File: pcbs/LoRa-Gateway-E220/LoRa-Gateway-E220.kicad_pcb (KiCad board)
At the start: 2 copper layers, 65.4 x 63 mm, 15 parts, among them J1 Conn_01x02, U1 ESP32_DevKit_V1_DOIT, U2 E-Byte-E220-900T22S, U3 QuinLED-ESP32-ETH-Hat

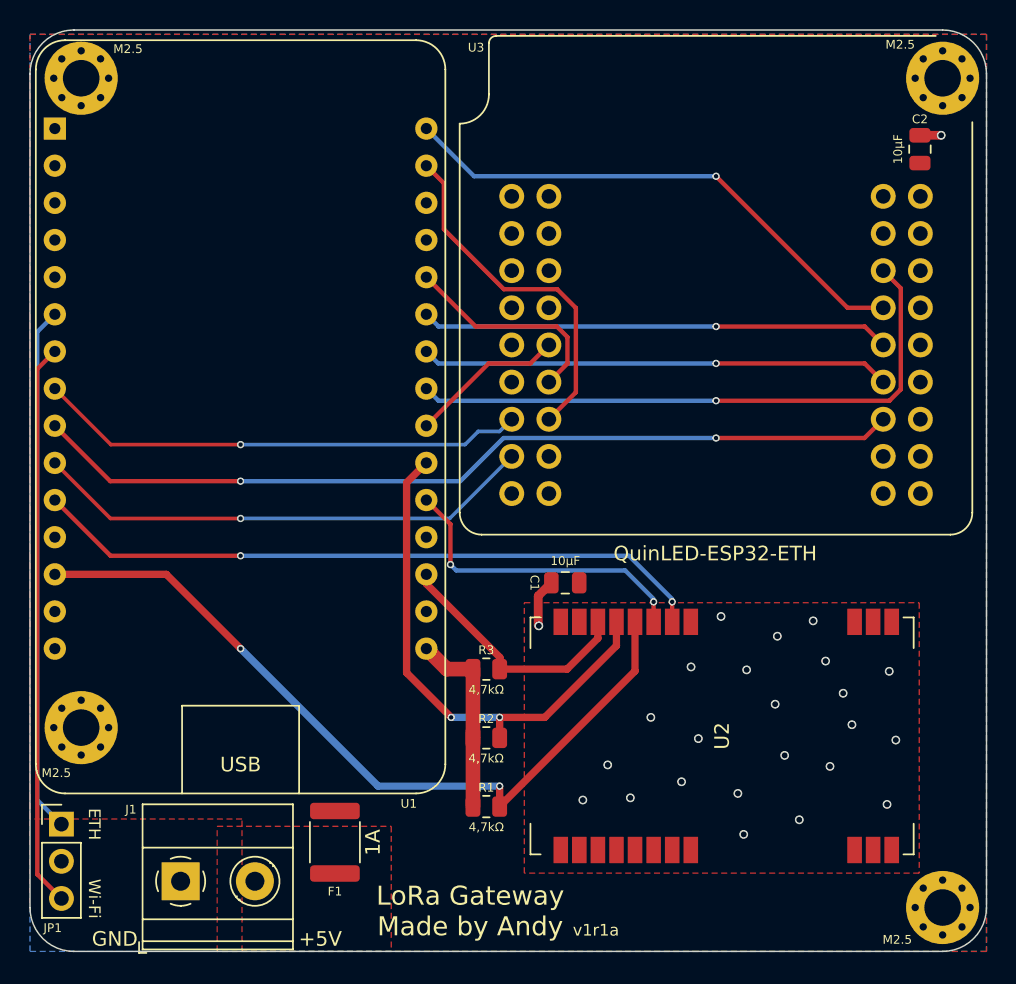
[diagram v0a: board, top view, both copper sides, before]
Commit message: Added iBOM, last small edits on both PCBs
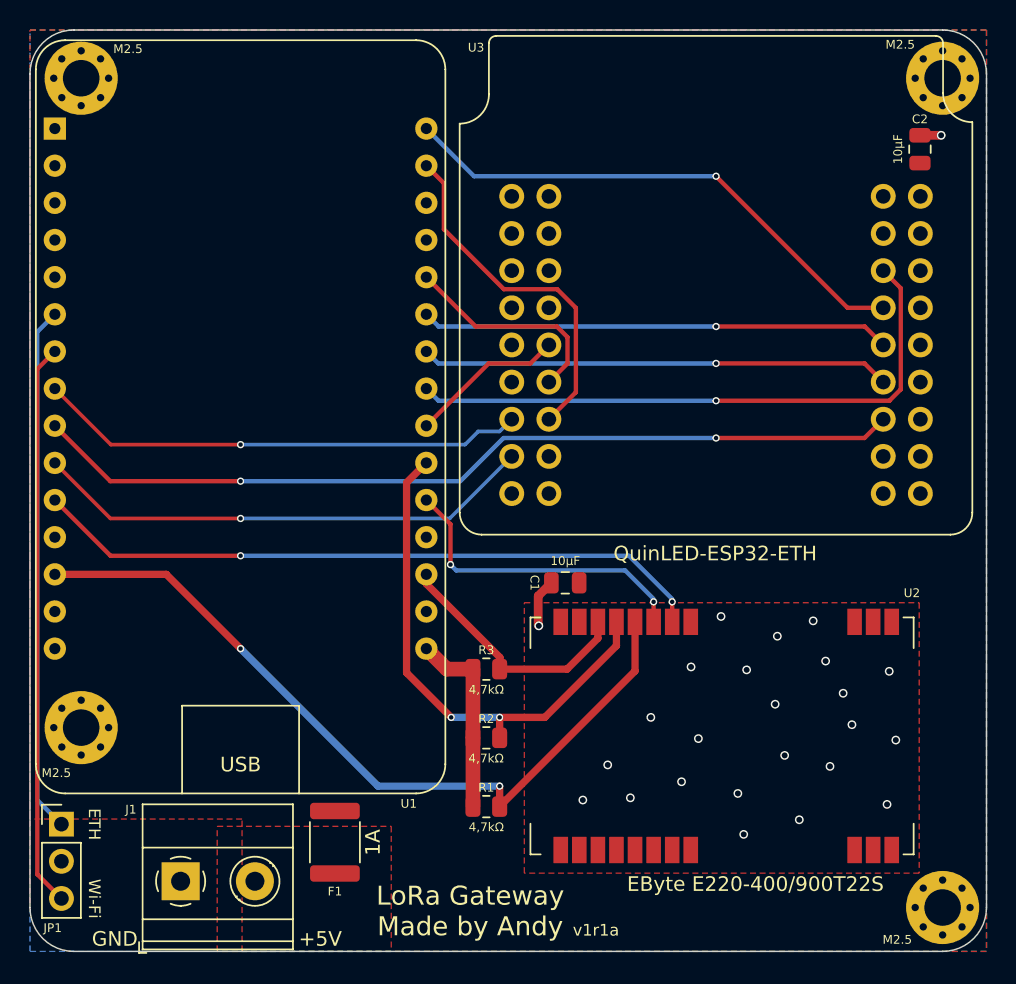
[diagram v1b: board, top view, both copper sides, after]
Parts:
- U2: value E-Byte-E220-900T22S -> EByte E220-400/900T22S
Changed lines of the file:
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@@
   )
   (paper "A4")
+  (title_block
+    (title "LoRa-Gateway-E220")
+    (rev "v1r1a")
+  )
   (layers
     (0 "F.Cu" signal)
@@
       (effects (font (size 1 1) (thickness 0.2)))
     )
+    (fp_line (start 2.5 34.1) (end 32.55 34.1) (layer "F.SilkS") (width 0.12))
+    (fp_line (start 2 30.2) (end 2 33.6) (layer "F.SilkS") (width 0.12))
     (fp_line (start 33.05 30.1) (end 33.05 33.6) (layer "F.SilkS") (width 0.12))
     (fp_line (start 1.5 0) (end 33.55 0) (layer "F.SilkS") (width 0.12))
-    (fp_line (start 2.5 34.1) (end 32.55 34.1) (layer "F.SilkS") (width 0.12))
     (fp_line (start 0 1.5) (end 0 28.2) (layer "F.SilkS") (width 0.12))
     (fp_line (start 35.05 1.5) (end 35.05 28.1) (layer "F.SilkS") (width 0.12))
     (fp_arc (start 33.05 33.6) (mid 32.903553 33.953553) (end 32.55 34.1) (layer "F.SilkS") (width 0.12))
+    (fp_arc (start 0 28.2) (mid 1.414214 28.785786) (end 2 30.2) (layer "F.SilkS") (width 0.12))
+    (fp_arc (start 0 1.5) (mid 0.43934 0.43934) (end 1.5 0) (layer "F.SilkS") (width 0.12))
     (fp_arc (start 33.05 30.1) (mid 33.635786 28.685786) (end 35.05 28.1) (layer "F.SilkS") (width 0.12))
+    (fp_arc (start 2.5 34.1) (mid 2.146447 33.953553) (end 2 33.6) (layer "F.SilkS") (width 0.12))
     (fp_arc (start 33.55 0) (mid 34.61066 0.43934) (end 35.05 1.5) (layer "F.SilkS") (width 0.12))
-    (fp_arc (start 0 1.5) (mid 0.43934 0.43934) (end 1.5 0) (layer "F.SilkS") (width 0.12))
     (pad "1" thru_hole circle (at 3.55 23.13 180) (size 1.7 1.7) (drill 1) (layers *.Cu *.Mask)
       (net 36 "5vF") (pinfunction "VCC") (pintype "input"))
@@
     (pad "35" thru_hole circle (at 28.95 23.13 180) (size 1.7 1.7) (drill 1) (layers *.Cu *.Mask))
     (pad "36" thru_hole circle (at 31.49 23.13 180) (size 1.7 1.7) (drill 1) (layers *.Cu *.Mask))
+    (model "C:/Users/andy/Documents/KiCad/3D Models/QuinLED-ESP32-Ethernet_v3r1.wrl"
+      (offset (xyz -110.9 65.8 8))
+      (scale (xyz 394 394 394))
+      (rotate (xyz 0 0 0))
+    )
   )
   (footprint "MountingHole:MountingHole_2.5mm_Pad_Via" (layer "F.Cu")
@@
     (property "Sheetname" "")
     (attr smd)
-    (fp_text reference "U2" (at 9.4 13.5 90) (layer "F.SilkS")
-      (effects (font (size 1 1) (thickness 0.15)))
-    )
-    (fp_text value "E-Byte-E220-900T22S" (at 9.4 27.95 90) (layer "F.Fab")
-      (effects (font (size 1 1) (thickness 0.15)))
+    (fp_text reference "U2" (at 19.1675 26.48 180) (layer "F.SilkS")
+      (effects (font (size 0.6 0.6) (thickness 0.12)))
+    )
+    (fp_text value "EByte E220-400/900T22S" (at -0.7325 15.78 180) (layer "F.SilkS")
+      (effects (font (size 1 1) (thickness 0.2)))
     )
     (fp_line (start 17.5 0.4) (end 17.5 1.1) (layer "F.SilkS") (width 0.12))
@@
     (fp_line (start 2.25 1.6) (end -2.25 1.6) (layer "F.Fab") (width 0.1))
     (fp_line (start -2.25 -1.6) (end 2.25 -1.6) (layer "F.Fab") (width 0.1))
-    (pad "1" smd roundrect locked (at -2.1375 0 270) (size 1.125 3.4) (layers "F.Cu" "F.Paste" "F.Mask") (roundrect_rratio 0.2222222222)
+    (pad "1" smd roundrect (at -2.1375 0 270) (size 1.125 3.4) (layers "F.Cu" "F.Paste" "F.Mask") (roundrect_rratio 0.2222222222)
       (net 36 "5vF") (pintype "passive"))
-    (pad "2" smd roundrect locked (at 2.1375 0 270) (size 1.125 3.4) (layers "F.Cu" "F.Paste" "F.Mask") (roundrect_rratio 0.2222222222)
+    (pad "2" smd roundrect (at 2.1375 0 270) (size 1.125 3.4) (layers "F.Cu" "F.Paste" "F.Mask") (roundrect_rratio 0.2222222222)
       (net 37 "/5V") (pintype "passive"))
     (model "${KICAD6_3DMODEL_DIR}/Fuse.3dshapes/Fuse_1812_4532Metric.wrl"
       (offset (xyz 0 0 0))
       (scale (xyz 1 1 1))
+      (rotate (xyz 0 0 0))
+    )
+    (model "${KICAD6_3DMODEL_DIR}/Fuse.3dshapes/Fuse_0805_2012Metric.wrl"
+      (offset (xyz 0 0 0))
+      (scale (xyz 2.5 2.5 2.5))
       (rotate (xyz 0 0 0))
     )
@@
         (xy 111.5 89.95)
         (xy 97 89.95)
-        (xy 97 36.3)
-        (xy 162.4 36.3)
+        (xy 97 36)
+        (xy 162.4 36)
       )
     )
@@
         (xy 162.4 99)
         (xy 97 99)
-        (xy 97 36.3)
-        (xy 162.4 36.3)
+        (xy 97 36)
+        (xy 162.4 36)
       )
     )
